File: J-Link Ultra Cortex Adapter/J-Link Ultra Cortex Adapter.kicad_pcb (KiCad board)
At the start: 2 copper layers, 37.5 x 36.1 mm, 5 parts, among them J1 SFH11-PBPC-D10-RA-BK, J2 3221-20-0300-00, J3 Conn_01x10, J4 3221-14-0300-00

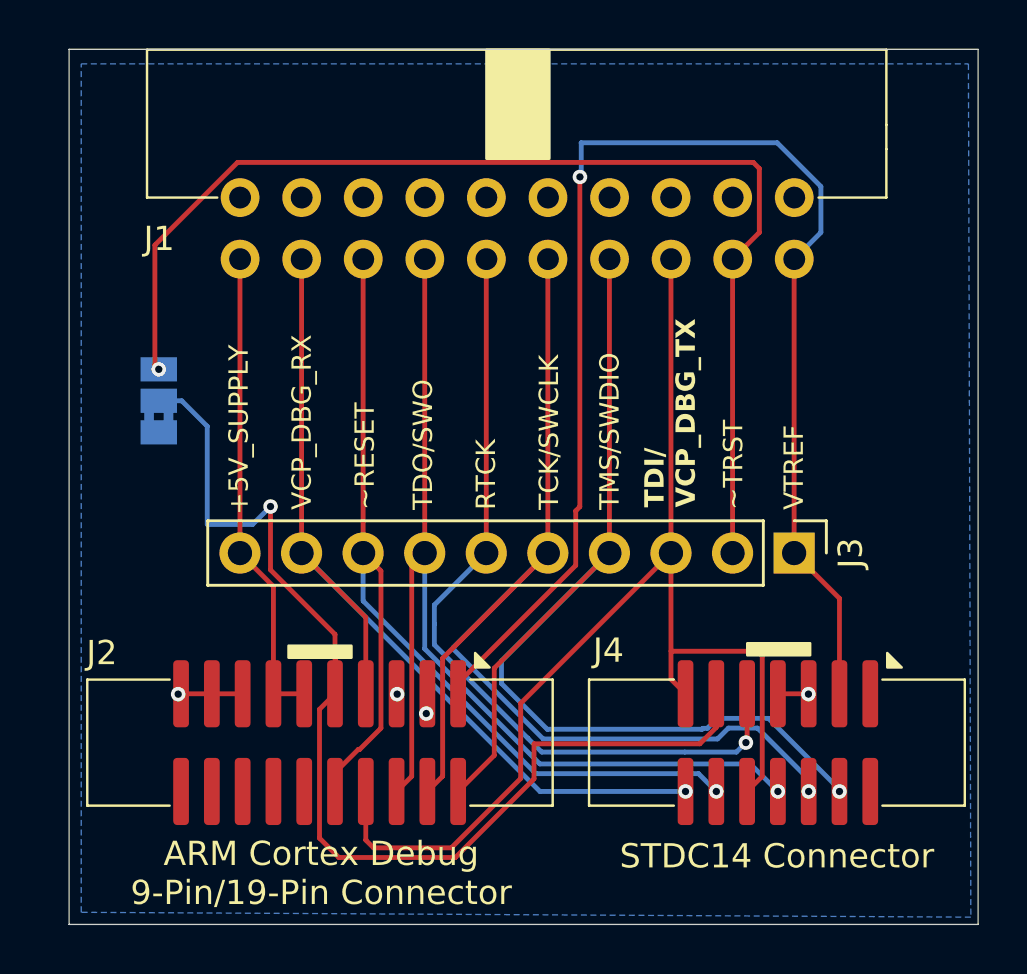
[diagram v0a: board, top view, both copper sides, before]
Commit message: Add PCBWay design rules
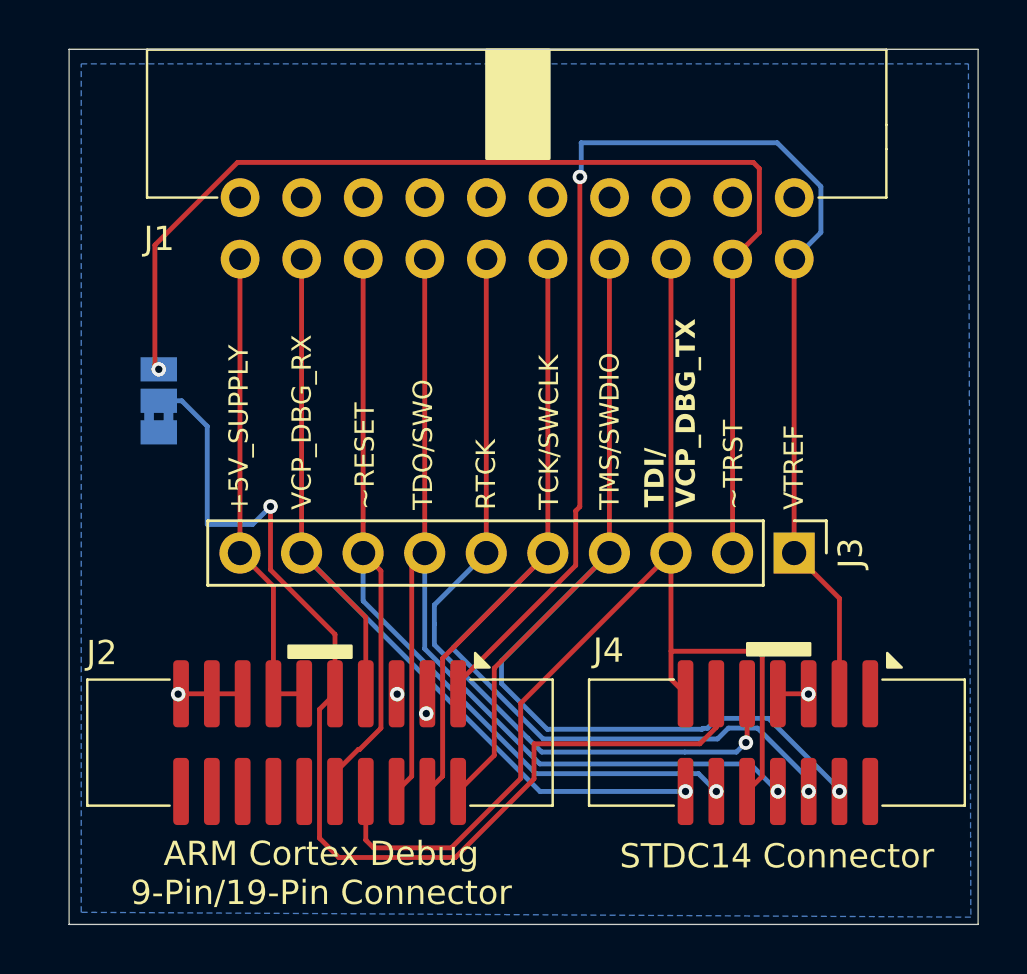
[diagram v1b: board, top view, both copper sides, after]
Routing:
- net /GNDDetect: track 47.2 -> 45.6 mm
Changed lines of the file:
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@@
 	)
 	(setup
+		(stackup
+			(layer "F.SilkS"
+				(type "Top Silk Screen")
+			)
+			(layer "F.Paste"
+				(type "Top Solder Paste")
+			)
+			(layer "F.Mask"
+				(type "Top Solder Mask")
+				(thickness 0.01)
+			)
+			(layer "F.Cu"
+				(type "copper")
+				(thickness 0.035)
+			)
+			(layer "dielectric 1"
+				(type "core")
+				(thickness 1.51)
+				(material "FR4")
+				(epsilon_r 4.5)
+				(loss_tangent 0.02)
+			)
+			(layer "B.Cu"
+				(type "copper")
+				(thickness 0.035)
+			)
+			(layer "B.Mask"
+				(type "Bottom Solder Mask")
+				(thickness 0.01)
+			)
+			(layer "B.Paste"
+				(type "Bottom Solder Paste")
+			)
+			(layer "B.SilkS"
+				(type "Bottom Silk Screen")
+			)
+			(copper_finish "None")
+			(dielectric_constraints no)
+		)
 		(pad_to_mask_clearance 0)
 		(allow_soldermask_bridges_in_footprints no)
@@
 				(font
 					(size 1 1)
-					(thickness 0.1)
+					(thickness 0.15)
 				)
 			)
@@
 				(font
 					(size 1 1)
-					(thickness 0.1)
+					(thickness 0.15)
 				)
 			)
@@
 				(font
 					(size 1 1)
-					(thickness 0.1)
+					(thickness 0.15)
 				)
 			)
@@
 	)
 	(segment
-		(start 109.519999 104.45)
-		(end 102.68 104.45)
+		(start 94.47 99.934314)
+		(end 94.47 102.385)
 		(width 0.2)
 		(layer "F.Cu")
@@
 	)
 	(segment
-		(start 94.47 99.934314)
-		(end 94.47 102.385)
+		(start 109.519999 104.45)
+		(end 102.68 104.45)
 		(width 0.2)
 		(layer "F.Cu")
@@
 	)
 	(segment
+		(start 91.81 97.274314)
+		(end 94.47 99.934314)
+		(width 0.2)
+		(layer "F.Cu")
+		(net 18)
+	)
+	(segment
 		(start 94.63 109.14)
 		(end 93.83 108.34)
@@
 	)
 	(segment
-		(start 91.81 97.274314)
-		(end 94.47 99.934314)
-		(width 0.2)
-		(layer "F.Cu")
-		(net 18)
-	)
-	(segment
 		(start 93.83 108.34)
 		(end 93.83 103.025)
@@
 		(width 0.2)
 		(layer "F.Cu")
-		(net 18)
-	)
-	(segment
-		(start 94.49 102.365)
-		(end 94.49 100.8)
-		(width 0.2)
-		(layer "F.Cu")

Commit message: Add stencil alignment holes
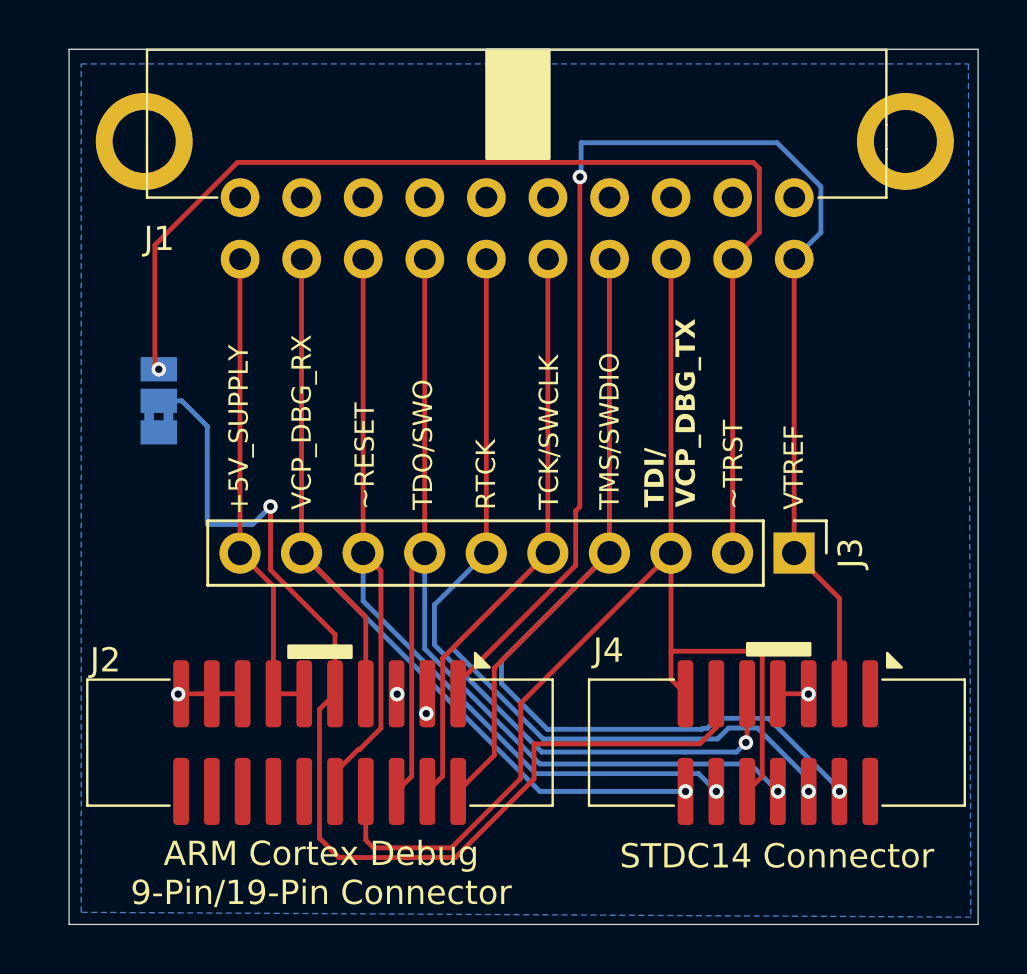
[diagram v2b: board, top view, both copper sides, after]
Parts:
- added H1: 2.6mm, ProjectLibrary:StencilAlignmentHole, F.Cu at (86.6, 79.6)
- added H2: 2.6mm, ProjectLibrary:StencilAlignmentHole, F.Cu at (118.0, 79.6)
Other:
- board text added: "2"
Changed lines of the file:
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@@
 	)
 	(property "date" "2024-07-27")
-	(property "version" "af208ec")
+	(property "version" "8a1d18b")
 	(net 0 "")
 	(net 1 "GND")
@@
 		)
 	)
+	(footprint "ProjectLibrary:StencilAlignmentHole"
+		(layer "F.Cu")
+		(at 118 79.6)
+		(property "Reference" "H2"
+			(at -2.54 -2.54 0)
+			(unlocked yes)
+			(layer "F.SilkS")
+			(hide yes)
+			(effects
+				(font
+					(size 1 1)
+					(thickness 0.1)
+				)
+			)
+		)
+		(property "Value" "2.6mm"
+			(at 0 5.08 0)
+			(unlocked yes)
+			(layer "F.Fab")
+			(effects
+				(font
+					(size 1 1)
+					(thickness 0.15)
+				)
+			)
+		)
+		(property "Footprint" "ProjectLibrary:StencilAlignmentHole"
+			(at 0 0 0)
+			(unlocked yes)
+			(layer "F.Fab")
+			(hide yes)
+			(effects
+				(font
+					(size 1 1)
+					(thickness 0.15)
+				)
+			)
+		)
+		(property "Datasheet" ""
+			(at 0 0 0)
+			(unlocked yes)
+			(layer "F.Fab")
+			(hide yes)
+			(effects
+				(font
+					(size 1 1)
+					(thickness 0.15)
+				)
+			)
+		)
+		(property "Description" ""
+			(at 0 6.35 0)
+			(unlocked yes)
+			(layer "F.Fab")
+			(hide yes)
+			(effects
+				(font
+					(size 1 1)
+					(thickness 0.15)
+				)
+			)
+		)
+		(sheetname "Root")
+		(sheetfile "J-Link Ultra Cortex Adapter.kicad_sch")
+		(attr through_hole exclude_from_bom)
+		(fp_text user "${REFERENCE}"
+			(at 0 3.81 0)
+			(unlocked yes)
+			(layer "F.Fab")
+			(effects
+				(font
+					(size 1 1)
+					(thickness 0.15)
+				)
+			)
+		)
+		(pad "1" smd circle
+			(at 0 0)
+			(size 2.6 2.6)
+			(layers "F.Cu" "F.Paste" "F.Mask")
+			(net 1 "GND")
+			(pintype "passive")
+		)
+		(pad "1" thru_hole circle
+			(at 0 0)
+			(size 4 4)
+			(drill 2.6)
+			(layers "*.Cu" "*.Mask")
+			(remove_unused_layers no)
+			(net 1 "GND")
+			(pintype "passive")
+		)
+	)
+	(footprint "ProjectLibrary:StencilAlignmentHole"
+		(layer "F.Cu")
+		(at 86.6 79.6)
+		(property "Reference" "H1"
+			(at -2.54 -2.54 0)
+			(unlocked yes)
+			(layer "F.SilkS")
+			(hide yes)
+			(effects
+				(font
+					(size 1 1)
+					(thickness 0.1)
+				)
+			)
+		)
+		(property "Value" "2.6mm"
+			(at 0 5.08 0)
+			(unlocked yes)
+			(layer "F.Fab")
+			(effects
+				(font
+					(size 1 1)
+					(thickness 0.15)
+				)
+			)
+		)
+		(property "Footprint" "ProjectLibrary:StencilAlignmentHole"
+			(at 0 0 0)
+			(unlocked yes)
+			(layer "F.Fab")
+			(hide yes)
+			(effects
+				(font
+					(size 1 1)
+					(thickness 0.15)
+				)
+			)
+		)
+		(property "Datasheet" ""
+			(at 0 0 0)
+			(unlocked yes)
+			(layer "F.Fab")
+			(hide yes)
+			(effects
+				(font
+					(size 1 1)
+					(thickness 0.15)
+				)
+			)
+		)
+		(property "Description" ""
+			(at 0 6.35 0)
+			(unlocked yes)
+			(layer "F.Fab")
+			(hide yes)
+			(effects
+				(font
+					(size 1 1)
+					(thickness 0.15)
+				)
+			)
+		)
+		(sheetname "Root")
+		(sheetfile "J-Link Ultra Cortex Adapter.kicad_sch")
+		(attr through_hole exclude_from_bom)
+		(fp_text user "${REFERENCE}"
+			(at 0 3.81 0)
+			(unlocked yes)
+			(layer "F.Fab")
+			(effects
+				(font
+					(size 1 1)
+					(thickness 0.15)
+				)
+			)
+		)
+		(pad "1" smd circle
+			(at 0 0)
+			(size 2.6 2.6)
+			(layers "F.Cu" "F.Paste" "F.Mask")
+			(net 1 "GND")
+			(pintype "passive")
+		)
+		(pad "1" thru_hole circle
+			(at 0 0)
+			(size 4 4)
+			(drill 2.6)
+			(layers "*.Cu" "*.Mask")
+			(remove_unused_layers no)
+			(net 1 "GND")
+			(pintype "passive")
+		)
+	)
 	(footprint "ProjectLibrary:SFH11-PBPC-D10-RA-BK"
 		(layer "F.Cu")
@@
 		(descr "20 Pin 0.05\" Pitch IDC Ribbon Cable Connector")
 		(property "Reference" "J2"
-			(at -14.7 -3.7 0)
+			(at -14.55 -3.4 0)
 			(unlocked yes)
 			(layer "F.SilkS")
@@
 		(tags "net tie solder jumper bridged")
 		(property "Reference" "JP1"
-			(at -0.1 -2 90)
+			(at -4.7 0 90)
 			(layer "B.SilkS")
+			(hide yes)
 			(effects
 				(font
@@
 			(layer "B.CrtYd")
 		)
+		(fp_text user "3"
+			(at 1.3 -2 -90)
+			(layer "B.SilkS")
+			(effects
+				(font
+					(size 1 1)
+					(thickness 0.15)
+				)
+				(justify mirror)
+			)
+		)
 		(fp_text user "1"
-			(at -2.6 0 -90)
-			(layer "B.SilkS")
-			(effects
-				(font
-					(size 1 1)
-					(thickness 0.15)
-				)
-				(justify mirror)
-			)
-		)
-		(fp_text user "3"
-			(at 2.6 0 -90)
+			(at -1.3 -2 -90)
 			(layer "B.SilkS")
 			(effects
@@
 	)
 	(gr_text "GNDDetect Jumper (JP1)\n1-2 connected (default) = GNDDetect grounded\n2-3 connected = GNDDetect connected to TRST"
-		(at 89.6 92 0)
+		(at 88.6 92.2 0)
 		(layer "B.SilkS")
 		(effects
@@
 		)
 	)
+	(gr_text "2"
+		(at 85.8 90.2 90)
+		(layer "B.SilkS")
+		(effects
+			(font
+				(size 1 1)
+				(thickness 0.15)
+			)
+			(justify bottom mirror)
+		)
+	)
